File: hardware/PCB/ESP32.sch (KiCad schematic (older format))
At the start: 1 part

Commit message: started ESP32 Schematic
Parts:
- added AE?: Antenna, symbol Device:Antenna
- added C?: 10u, Capacitor_SMD:C_0603_1608Metric, symbol Device:C
- added C?: 1u, Capacitor_SMD:C_0603_1608Metric, symbol Device:C
- added C? (x7): 100n, Capacitor_SMD:C_0603_1608Metric, symbol Device:C
- added C?: 10n, Capacitor_SMD:C_0603_1608Metric, symbol Device:C
- added C?: 3n3, Capacitor_SMD:C_0603_1608Metric, symbol Device:C
- added C? (x2): TBD, Capacitor_SMD:C_0603_1608Metric, symbol Device:C
- added L?: 2n, Inductor_SMD:L_0603_1608Metric, symbol pspice:INDUCTOR
- added L?: 0R, Inductor_SMD:L_0603_1608Metric, symbol pspice:INDUCTOR
- added R?: 20k, Resistor_SMD:R_0603_1608Metric, symbol Device:R
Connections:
- net labels added: +3V3, GND
- wire segments 0 -> 69
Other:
- moved on the sheet: IC?

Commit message: add mechannical and usb ftdi sheet
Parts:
- gave numbers to parts that had none: 18

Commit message: add 32khz crystal for rtc
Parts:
- added C38, C39: 12p5, Capacitor_SMD:C_0603_1608Metric, symbol Device:C
- added Y1: ABS05-32.768KHZ-T, ProjectFootprints:ABS05, symbol ABS05-32.768KHZ-T:ABS05-32.768KHZ-T
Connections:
- net labels added: 32K_XN, 32K_XP
- wire segments 69 -> 79
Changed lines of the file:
@@
 $Descr A4 11693 8268
 encoding utf-8
-Sheet 6 7
+Sheet 5 7
 Title ""
 Date ""
@@
 	6100 5550 6600 5550
 Connection ~ 6600 5550
+$Comp
+L ABS05-32.768KHZ-T:ABS05-32.768KHZ-T Y1
+U 1 1 5FE918FF
+P 1300 6750
+F 0 "Y1" H 1800 6900 50  0000 L CNN
+F 1 "ABS05-32.768KHZ-T" H 1700 6450 50  0000 C CNN
+F 2 "ProjectFootprints:ABS05" H 1950 6850 50  0001 L CNN
+F 3 "" H 1950 6750 50  0001 L CNN
+F 4 "ABRACON - ABS05-32.768KHZ-T - CRYSTAL, 32.768KHZ, 12.5PF, 1.6 X 1MM" H 1950 6650 50  0001 L CNN "Description"
+F 5 "" H 1950 6550 50  0001 L CNN "Height"
+F 6 "815-ABS05-32.768K-T" H 1950 6450 50  0001 L CNN "Mouser Part Number"
+F 7 "https://www.mouser.co.uk/ProductDetail/ABRACON/ABS05-32768KHZ-T/?qs=Pyu0ZBy%2FIJZ5hxIXB%2FLU5A%3D%3D" H 1950 6350 50  0001 L CNN "Mouser Price/Stock"
+F 8 "ABRACON" H 1950 6250 50  0001 L CNN "Manufacturer_Name"
+F 9 "ABS05-32.768KHZ-T" H 1950 6150 50  0001 L CNN "Manufacturer_Part_Number"
+	1    1300 6750
+	-1   0    0    -1
+$EndComp
+$Comp
+L Device:C C?
+U 1 1 5FE97E75
+P 1500 7250
+AR Path="/5FE97E75" Ref="C?"  Part="1"
+AR Path="/5FCFD0E2/5FE97E75" Ref="C38"  Part="1"
+AR Path="/5FE895CA/5FE97E75" Ref="C?"  Part="1"
+F 0 "C38" H 1615 7296 50  0000 L CNN
+F 1 "12p5" H 1615 7205 50  0000 L CNN
+F 2 "Capacitor_SMD:C_0603_1608Metric" H 1538 7100 50  0001 C CNN
+F 3 "~" H 1500 7250 50  0001 C CNN
+	1    1500 7250
+	1    0    0    -1
+$EndComp
+$Comp
+L power:GND #PWR?
+U 1 1 5FE97E7B
+P 1500 7550
+AR Path="/5FE97E7B" Ref="#PWR?"  Part="1"
+AR Path="/5FCFD0E2/5FE97E7B" Ref="#PWR088"  Part="1"
+AR Path="/5FE895CA/5FE97E7B" Ref="#PWR?"  Part="1"
+F 0 "#PWR088" H 1500 7300 50  0001 C CNN
+F 1 "GND" H 1505 7377 50  0000 C CNN
+F 2 "" H 1500 7550 50  0001 C CNN
+F 3 "" H 1500 7550 50  0001 C CNN
+	1    1500 7550
+	1    0    0    -1
+$EndComp
+Wire Wire Line
+	1500 7400 1500 7550
+Wire Wire Line
+	1300 6850 1500 6850
+Wire Wire Line
+	1500 6850 1500 7100
+$Comp
+L Device:C C?
+U 1 1 5FE9B435
+P 2000 7250
+AR Path="/5FE9B435" Ref="C?"  Part="1"
+AR Path="/5FCFD0E2/5FE9B435" Ref="C39"  Part="1"
+AR Path="/5FE895CA/5FE9B435" Ref="C?"  Part="1"
+F 0 "C39" H 2115 7296 50  0000 L CNN
+F 1 "12p5" H 2115 7205 50  0000 L CNN
+F 2 "Capacitor_SMD:C_0603_1608Metric" H 2038 7100 50  0001 C CNN
+F 3 "~" H 2000 7250 50  0001 C CNN
+	1    2000 7250
+	1    0    0    -1
+$EndComp
+$Comp
+L power:GND #PWR?
+U 1 1 5FE9B43B
+P 2000 7550
+AR Path="/5FE9B43B" Ref="#PWR?"  Part="1"
+AR Path="/5FCFD0E2/5FE9B43B" Ref="#PWR089"  Part="1"
+AR Path="/5FE895CA/5FE9B43B" Ref="#PWR?"  Part="1"
+F 0 "#PWR089" H 2000 7300 50  0001 C CNN
+F 1 "GND" H 2005 7377 50  0000 C CNN
+F 2 "" H 2000 7550 50  0001 C CNN
+F 3 "" H 2000 7550 50  0001 C CNN
+	1    2000 7550
+	1    0    0    -1
+$EndComp
+Wire Wire Line
+	2000 7400 2000 7550
+Wire Wire Line
+	1300 6750 2000 6750
+Wire Wire Line
+	2000 6750 2000 7100
+Text GLabel 2350 6750 2    50   Output ~ 0
+32K_XP
+Text GLabel 2350 6850 2    50   Output ~ 0
+32K_XN
+Wire Wire Line
+	1500 6850 2350 6850
+Connection ~ 1500 6850
+Wire Wire Line
+	2000 6750 2350 6750
+Connection ~ 2000 6750
+Text GLabel 5000 3750 0    50   Input ~ 0
+32K_XP
+Text GLabel 5000 3850 0    50   Input ~ 0
+32K_XN
+Wire Wire Line
+	5000 3750 5300 3750
+Wire Wire Line
+	5000 3850 5300 3850
 $EndSCHEMATC

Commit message: add ESP32 antenna
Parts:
- removed AE1: Antenna, symbol Device:Antenna
- added U3: ESP32_Antenna, RF_Antenna:Texas_SWRA117D_2.4GHz_Right, symbol ProjectLibrary:ESP32_Antenna
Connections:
- wire segments 79 -> 80
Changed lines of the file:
@@
 Wire Wire Line
 	1400 3050 1400 3000
-Connection ~ 1400 3000
-Wire Wire Line
-	1400 3000 1000 3000
 Wire Wire Line
 	2150 3000 2350 3000
 Wire Wire Line
 	2350 3000 2350 3050
-$Comp
-L Device:Antenna AE1
-U 1 1 5FD37ECF
-P 1000 2700
-AR Path="/5FCFD0E2/5FD37ECF" Ref="AE1"  Part="1"
-AR Path="/5FE895CA/5FD37ECF" Ref="AE?"  Part="1"
-F 0 "AE1" H 1080 2689 50  0000 L CNN
-F 1 "Antenna" H 1080 2598 50  0000 L CNN
-F 2 "" H 1000 2700 50  0001 C CNN
-F 3 "~" H 1000 2700 50  0001 C CNN
-	1    1000 2700
-	1    0    0    -1
-$EndComp
-Wire Wire Line
-	1000 2900 1000 3000
 Wire Wire Line
 	5300 2750 2350 2750
@@
 Wire Wire Line
 	5000 3850 5300 3850
+$Comp
+L ProjectLibrary:ESP32_Antenna U3
+U 1 1 5FE9520D
+P 650 2950
+F 0 "U3" H 833 3125 50  0000 C CNN
+F 1 "ESP32_Antenna" H 833 3034 50  0000 C CNN
+F 2 "RF_Antenna:Texas_SWRA117D_2.4GHz_Right" H 650 3000 50  0001 C CNN
+F 3 "" H 650 3000 50  0001 C CNN
+	1    650  2950
+	1    0    0    -1
+$EndComp
+Wire Wire Line
+	1000 3000 1400 3000
+Connection ~ 1400 3000
+$Comp
+L power:GND #PWR?
+U 1 1 5FEA234E
+P 1100 3500
+AR Path="/5FEA234E" Ref="#PWR?"  Part="1"
+AR Path="/5FCFD0E2/5FEA234E" Ref="#PWR090"  Part="1"
+AR Path="/5FE895CA/5FEA234E" Ref="#PWR?"  Part="1"
+F 0 "#PWR090" H 1100 3250 50  0001 C CNN
+F 1 "GND" H 1105 3327 50  0000 C CNN
+F 2 "" H 1100 3500 50  0001 C CNN
+F 3 "" H 1100 3500 50  0001 C CNN
+	1    1100 3500
+	1    0    0    -1
+$EndComp
+Wire Wire Line
+	1000 3100 1100 3100
+Wire Wire Line
+	1100 3100 1100 3500
 $EndSCHEMATC

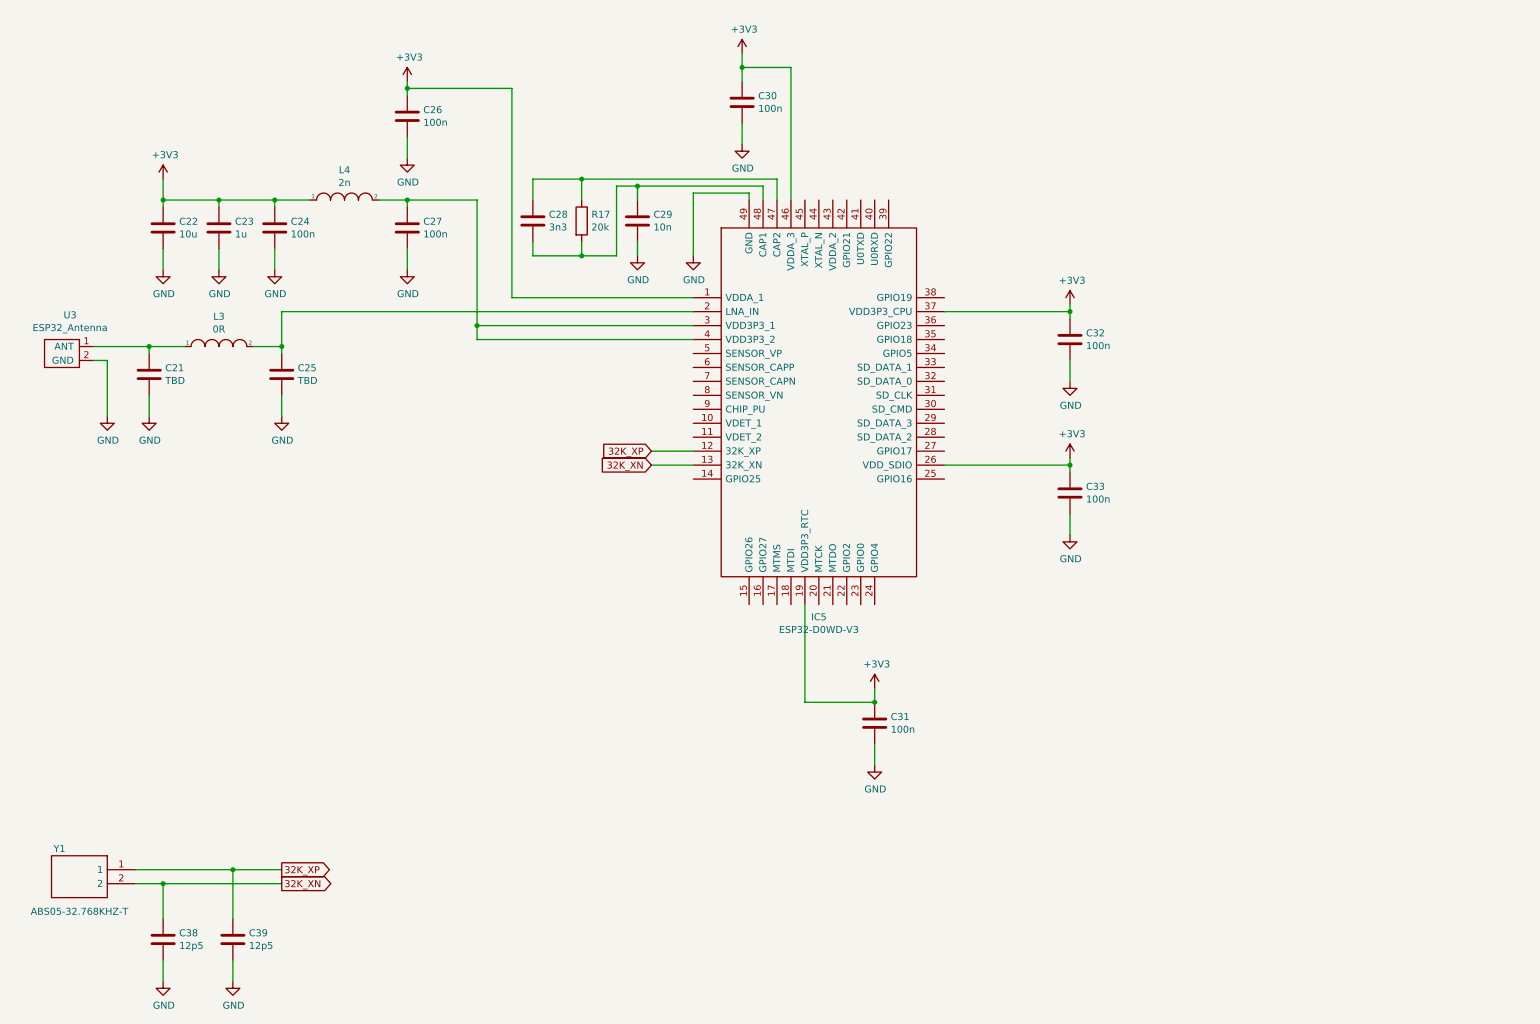
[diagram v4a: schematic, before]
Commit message: add 40 MHz crystal
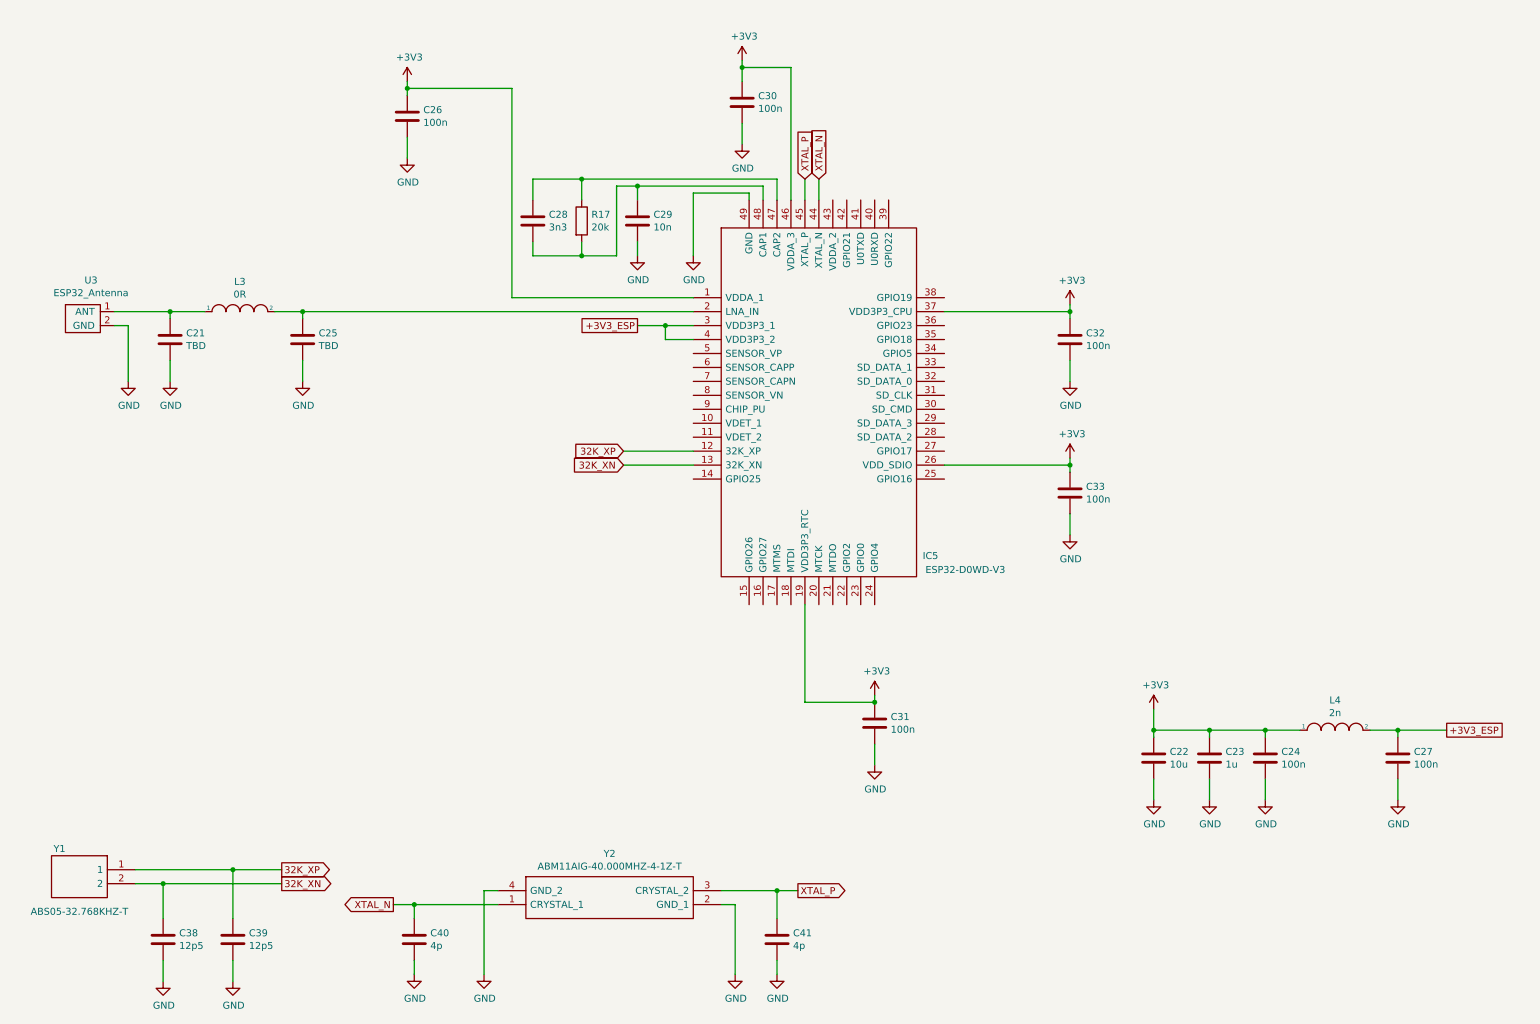
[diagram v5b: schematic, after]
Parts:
- added C40, C41: 4p, Capacitor_SMD:C_0603_1608Metric, symbol Device:C
- added Y2: ABM11AIG-40.000MHZ-4-1Z-T, ProjectFootprints:ABM11AIG40000MHZ41ZT, symbol ProjectLibrary:ABM11AIG-40.000MHZ-4-1Z-T
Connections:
- net GND: now also C40.2, C41.2, Y2.2 (GND_1), Y2.4 (GND_2)
- net +3V3_ESP: now reaches C27.1, IC5.3 (VDD3P3_1), IC5.4 (VDD3P3_2), L4.2
- net XTAL_N: now reaches IC5.44 (XTAL_N)
- net XTAL_N: now also C40.1, Y2.1 (CRYSTAL_1)
- net XTAL_P: now reaches IC5.45 (XTAL_P)
- net XTAL_P: now also C41.1, Y2.3 (CRYSTAL_2)
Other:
- moved on the sheet: C21, C22, C23, C24, C25, C27, L3, L4, U3
